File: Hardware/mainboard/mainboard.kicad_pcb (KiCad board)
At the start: 2 copper layers, 149.9 x 99.9 mm, 88 parts, among them IC1 DS1813, IC2 DS1813, J1 Barrel_Jack, J2 Conn_02x02_Odd_Even, J3 Conn_01x06, J4 Conn_01x14, SW1 SW, U1 74AC161, U2 L7905, U4 PAL24, U5 GAL16V8, U6 W65C02SxP, U7 HM62256BLP, U8 28C256, U9 W65C51NxP, X1 24MHz, X3 1.8432MHz

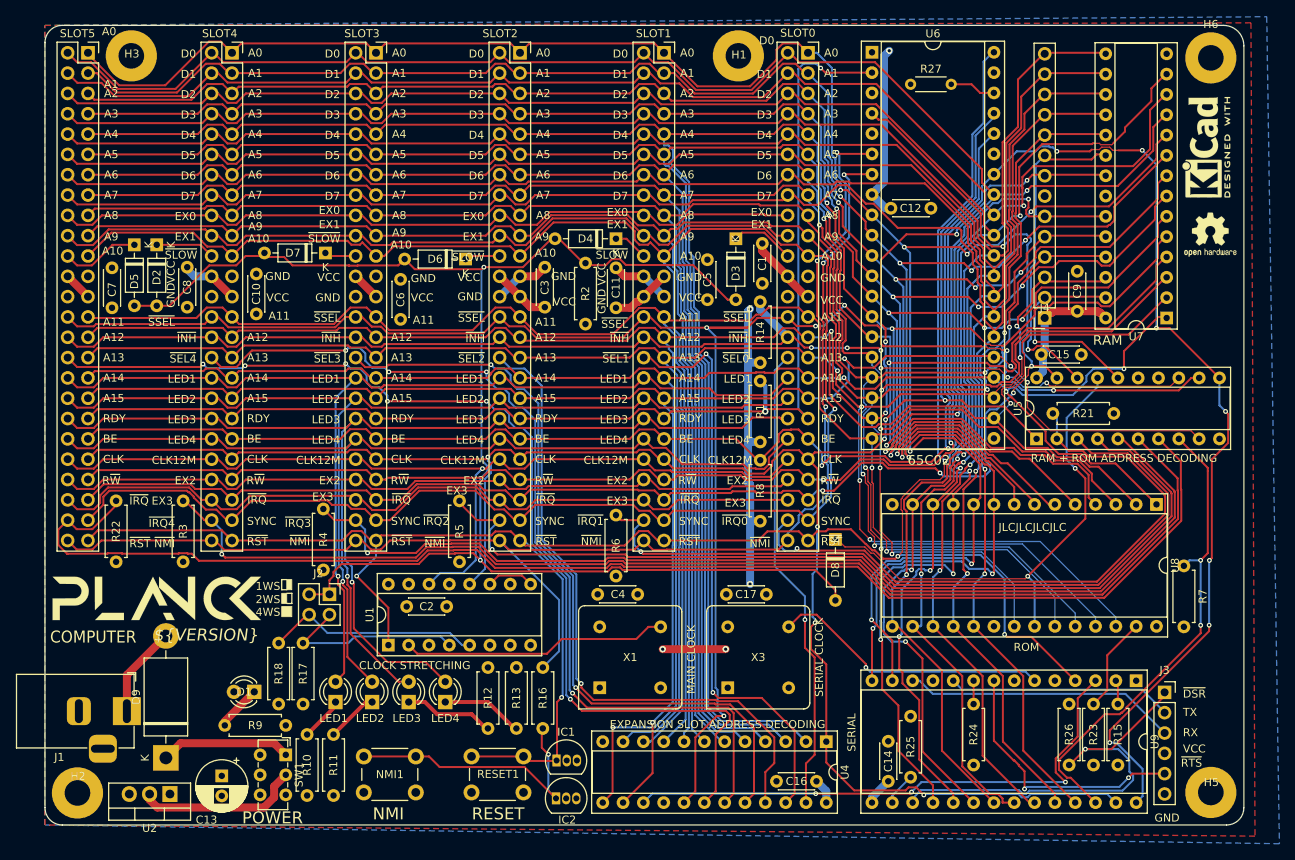
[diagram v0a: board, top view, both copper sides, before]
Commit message: Fix mainboard power + add A13 and A14 to RAM/ROM address decoding.
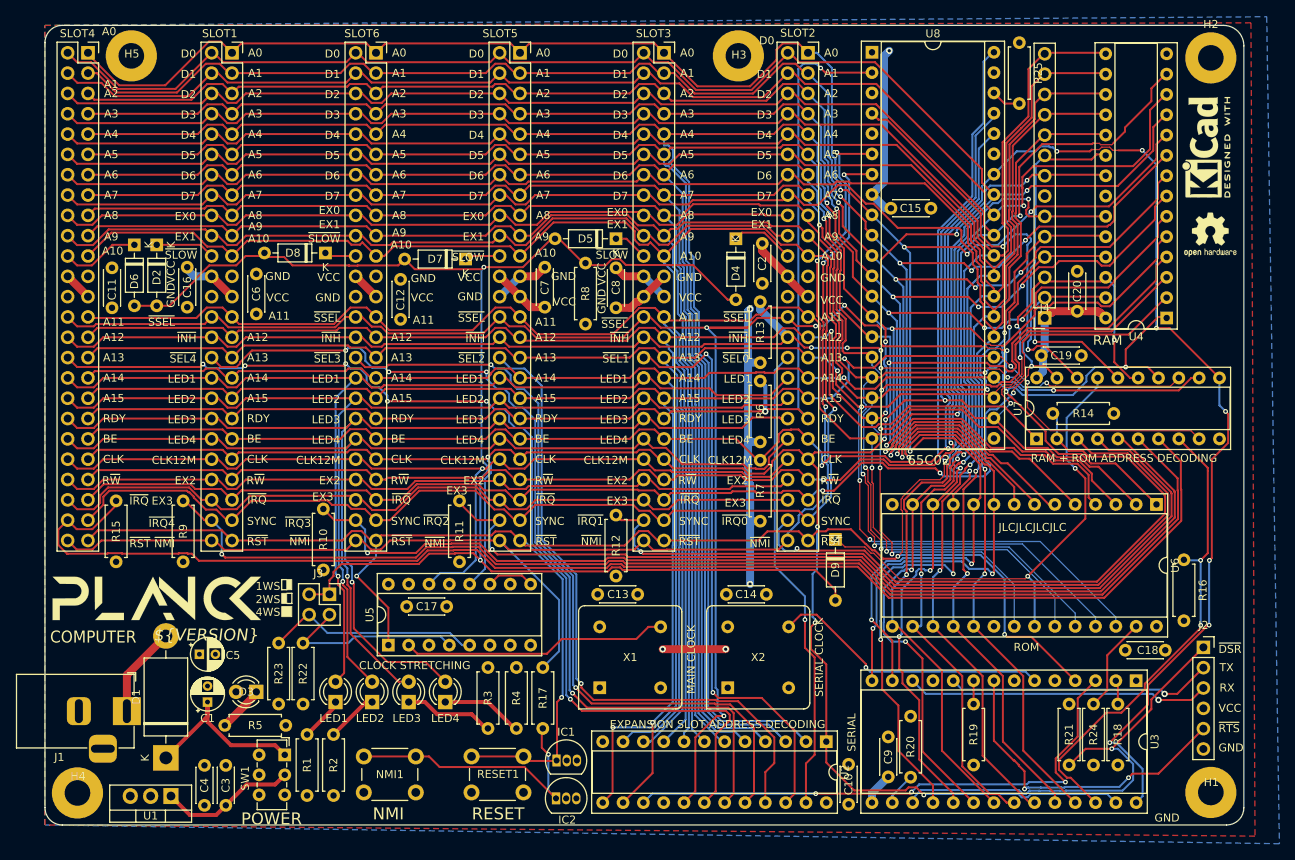
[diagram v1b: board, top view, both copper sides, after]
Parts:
- removed the U2 at (15.6, 96.1)
- added C3: .1u, Capacitor_THT:C_Disc_D4.3mm_W1.9mm_P5.00mm, F.Cu at (22.6, 97.5)
- added C4: .1u, Capacitor_THT:C_Disc_D4.3mm_W1.9mm_P5.00mm, F.Cu at (19.9, 97.5)
- added C5: 47u, Capacitor_THT:CP_Radial_D4.0mm_P2.00mm, F.Cu at (19.3, 78.6)
- added U1: L7805, Package_TO_SOT_THT:TO-220-3_Vertical, F.Cu at (15.7, 96.3)
- C1: renamed from C13; footprint Capacitor_THT:CP_Radial_D6.3mm_P2.50mm -> Capacitor_THT:CP_Radial_D4.0mm_P2.00mm
- C12: renamed from C6; value 47n -> 1u
- R25: renamed from R27; footprint Resistor_THT:R_Axial_DIN0204_L3.6mm_D1.6mm_P5.08mm_Horizontal -> Resistor_THT:R_Axial_DIN0207_L6.3mm_D2.5mm_P7.62mm_Horizontal
- U2: renamed from U4; value PAL24 -> AT22V10
- moved C19 47.3 mm to (129.5, 41.3), turned to 180 degrees
- moved C18 37.4 mm to (135.0, 78.1), turned to 0 degrees
- moved R25 14.6 mm to (121.8, 2.16), turned to -90 degrees
- moved C1 9.40 mm to (20.3, 84.6), turned to 90 degrees
- moved C10 9.26 mm to (100.5, 92.4), turned to -90 degrees
- moved J2 7.43 mm to (144.8, 77.7)
- moved R16 0.76 mm to (142.4, 66.8)
- moved C9 0.55 mm to (105.4, 93.9)
- moved D3 0.26 mm to (26.4, 83.3)
- moved SW1 0.13 mm to (30.0, 91.2)
- renumbered C16 to C10, C7 to C11, C4 to C13, C17 to C14, C12 to C15, C8 to C16, C2 to C17, C15 to C18, C5 to C19, C1 to C2, C9 to C20, C10 to C6, C3 to C7, C11 to C8, C14 to C9, D9 to D1, D1 to D3, D3 to D4, D4 to D5, D5 to D6, D6 to D7, D7 to D8, D8 to D9, H5 to H1, H6 to H2, H1 to H3, H2 to H4, H3 to H5, J3 to J2, J2 to J3, R10 to R1, R4 to R10, R5 to R11, R6 to R12, R14 to R13, R21 to R14, R22 to R15, R7 to R16, R16 to R17, R15 to R18, R24 to R19, R11 to R2, R25 to R20, R26 to R21, R17 to R22, R18 to R23, R23 to R24, R12 to R3, R13 to R4, R9 to R5, R1 to R6, R8 to R7, R2 to R8, R3 to R9, SLOT4 to SLOT1, SLOT0 to SLOT2, SLOT1 to SLOT3, SLOT5 to SLOT4, SLOT2 to SLOT5, SLOT3 to SLOT6, U9 to U3, U7 to U4, U1 to U5, U8 to U6, U5 to U7, U6 to U8, X3 to X2
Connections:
- C1 pad 1: +5V -> Net-(D1-Pad1)
- D1 pad 1: Net-(D9-Pad1) -> Net-(D1-Pad1)
- SW1 pad 1: Net-(D9-Pad1) -> Net-(D1-Pad1)
- U7 pad 14: unconnected-(U5-Pad14) -> A14
- U7 pad 15: unconnected-(U5-Pad15) (its old number) -> A13
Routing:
- net Net-(D1-Pad1): track 0.00 -> 23.0 mm
- net Net-(D9-Pad1): track 16.3 -> 0.00 mm
- net A13: track 253.5 -> 268.4 mm, vias 6 -> 7
- net /~{RTS}: track 33.9 -> 40.7 mm
- net /TX: track 28.0 -> 33.3 mm, vias 0 -> 1
- net A14: track 232.9 -> 237.6 mm
- net /~{DSR}: track 53.8 -> 58.0 mm
- net /RX: track 34.2 -> 38.0 mm, vias 0 -> 1
- net Net-(SW1-Pad2): track 20.6 -> 17.3 mm
- net +5V: track 127.2 -> 124.6 mm
- net Net-(R25-Pad2): track 5.78 -> 3.73 mm

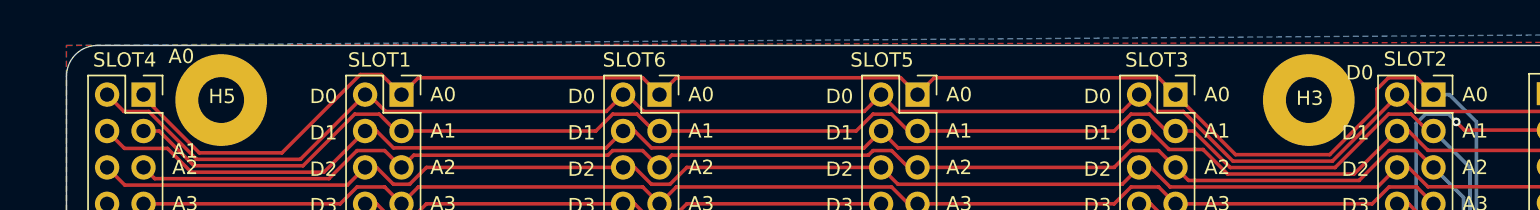
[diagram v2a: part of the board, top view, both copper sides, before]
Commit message: Change slot solder mask
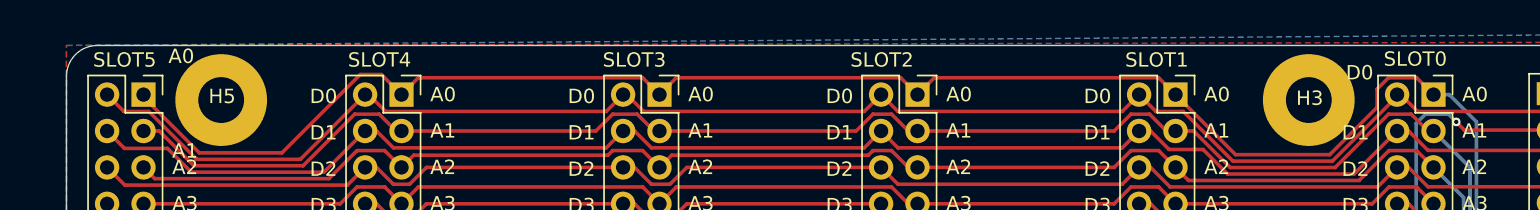
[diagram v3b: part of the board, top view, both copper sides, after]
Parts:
- renumbered SLOT2 to SLOT0, SLOT3 to SLOT1, SLOT5 to SLOT2, SLOT6 to SLOT3, SLOT1 to SLOT4, SLOT4 to SLOT5
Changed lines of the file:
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@@
     (property "Sheetname" "")
     (attr through_hole)
-    (fp_text reference "SLOT6" (at -1.753 -2.413) (layer "F.SilkS")
+    (fp_text reference "SLOT3" (at -1.753 -2.413) (layer "F.SilkS")
       (effects (font (size 1 1) (thickness 0.15)))
     )
@@
     (property "Sheetname" "")
     (attr through_hole)
-    (fp_text reference "SLOT1" (at -1.533 -2.413) (layer "F.SilkS")
+    (fp_text reference "SLOT4" (at -1.533 -2.413) (layer "F.SilkS")
       (effects (font (size 1 1) (thickness 0.15)))
     )
@@
     (property "Sheetname" "")
     (attr through_hole)
-    (fp_text reference "SLOT4" (at -1.313 -2.413) (layer "F.SilkS")
+    (fp_text reference "SLOT5" (at -1.313 -2.413) (layer "F.SilkS")
       (effects (font (size 1 1) (thickness 0.15)))
     )
@@
     (property "Sheetname" "")
     (attr through_hole)
-    (fp_text reference "SLOT3" (at -1.304 -2.413) (layer "F.SilkS")
+    (fp_text reference "SLOT1" (at -1.304 -2.413) (layer "F.SilkS")
       (effects (font (size 1 1) (thickness 0.15)))
     )
@@
     (property "Sheetname" "")
     (attr through_hole)
-    (fp_text reference "SLOT5" (at -2.481 -2.413) (layer "F.SilkS")
+    (fp_text reference "SLOT2" (at -2.481 -2.413) (layer "F.SilkS")
       (effects (font (size 1 1) (thickness 0.15)))
     )
@@
     (property "Sheetname" "")
     (attr through_hole)
-    (fp_text reference "SLOT2" (at -1.27 -2.4765) (layer "F.SilkS")
-      (effects (font (size 1 1) (thickness 0.15)))
-    )
+    (fp_text reference "SLOT0" (at -1.27 -2.4765) (layer "F.SilkS")
+      (effects (font (size 1 1) (thickness 0.15)))
+    )

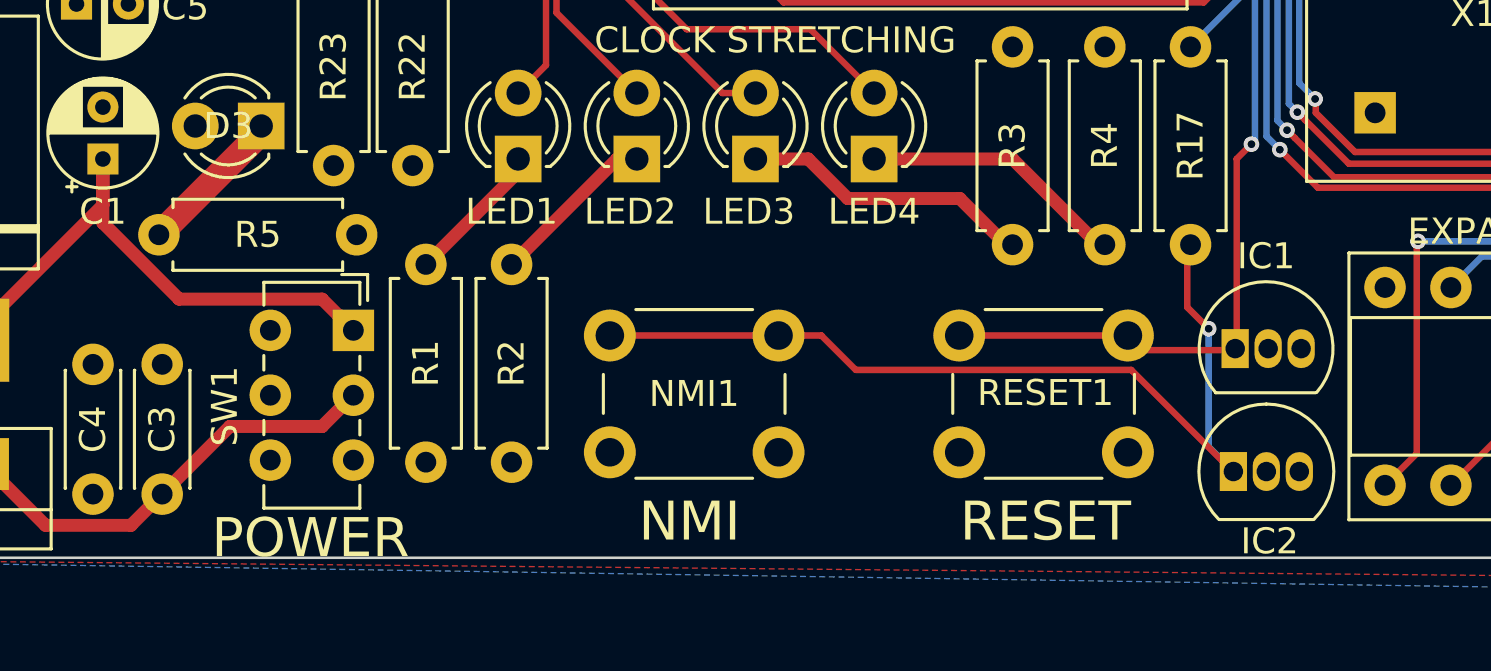
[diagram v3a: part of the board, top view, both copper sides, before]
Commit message: Fix mainboard DRC
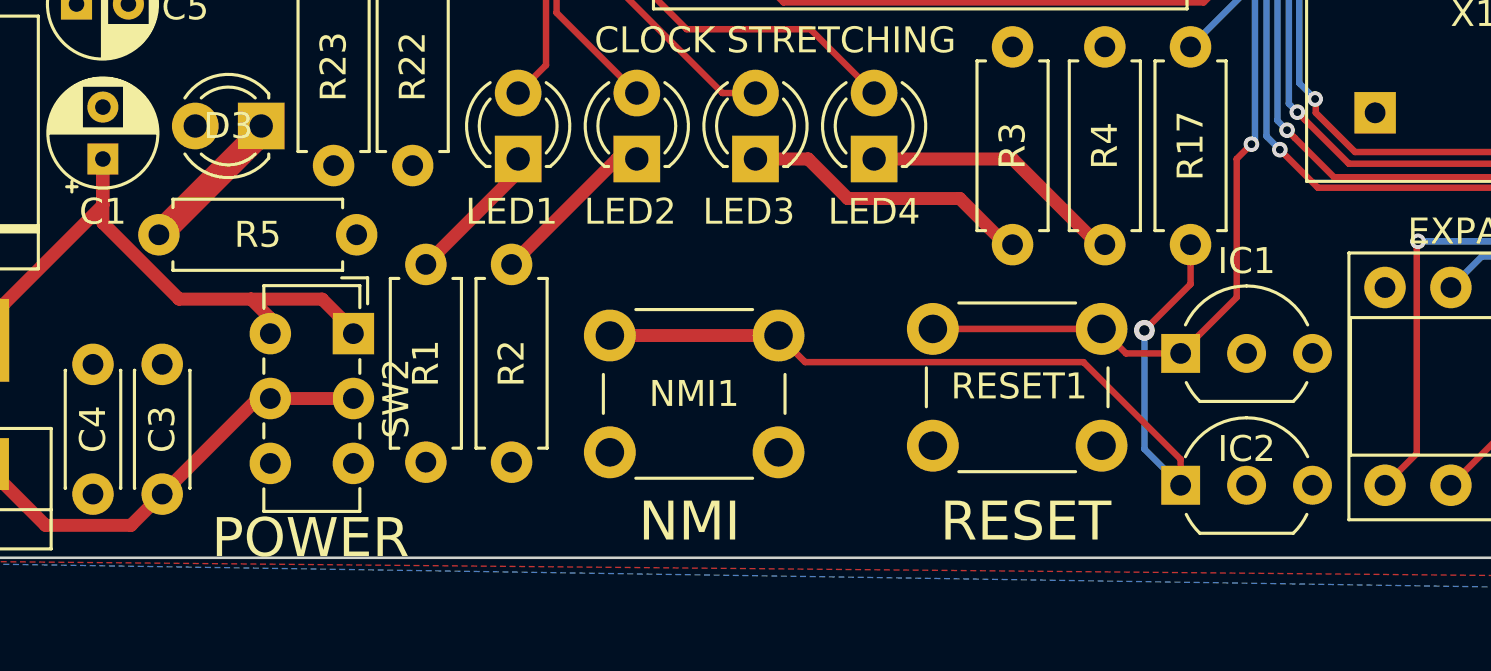
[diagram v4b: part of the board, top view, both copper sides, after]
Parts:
- removed SW1: SW, Button_Switch_THT:SW_E-Switch_EG1271_SPDT
- added SW2: SW_Push_DPDT, Button_Switch_THT:SW_E-Switch_EG1271_SPDT, F.Cu at (30.0, 91.3)
- IC1: footprint Package_TO_SOT_THT:TO-92L_Inline -> Package_TO_SOT_THT:TO-92_Inline_Wide
- IC2: footprint Package_TO_SOT_THT:TO-92_Inline -> Package_TO_SOT_THT:TO-92_Inline_Wide
- moved IC1 2.11 mm to (61.8, 92.1)
- moved IC2 2.10 mm to (61.8, 97.2)
- moved RESET1 1.05 mm to (58.8, 95.6)
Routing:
- net Net-(D1-K): track 23.0 -> 24.6 mm
- net ~{RESET}: track 267.0 -> 267.8 mm
